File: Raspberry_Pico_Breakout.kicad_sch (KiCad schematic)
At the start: 13 parts, among them J1 Conn_01x20, J2 Conn_01x20, J3 Conn_01x20, J4 Conn_01x20, J5 Conn_01x20, J6 Conn_01x20, J7 Conn_01x20, J8 Conn_01x20

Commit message: doc: updated part documentation, schematics readability
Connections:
- no-connect marks 160 -> 0
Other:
- note added: "Female Header"
- note added: "For user"
- note added: "Left Socket for Pico"
- note added: "M3 Mounting holes"
- note added: "Male Headers"
- note added: "Pico IO Board"
- note added: "Right Socket for Pico"
- moved on the sheet: A1, J5

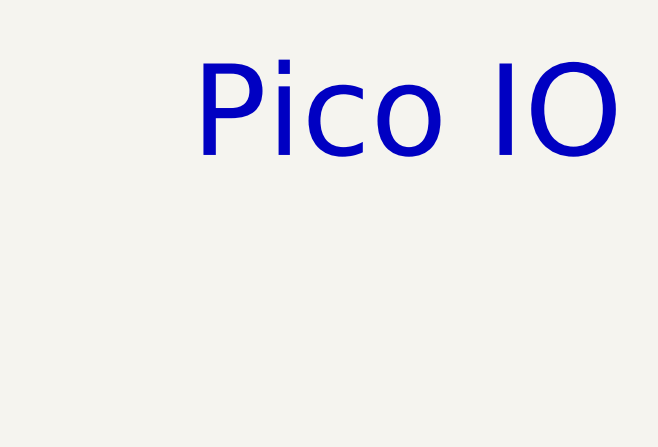
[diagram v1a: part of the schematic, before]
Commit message: doc: updated on schematic and PCB added license and design text
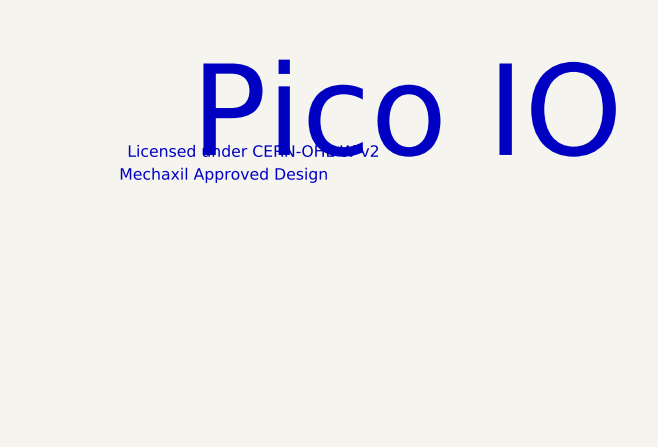
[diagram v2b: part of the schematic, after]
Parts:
- A1: now left out of the parts list
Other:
- note added: "Licensed under CERN-OHL-W v2"
- note added: "Mechaxil Approved Design"
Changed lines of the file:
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@@
 		)
 	)
+	(text "Licensed under CERN-OHL-W v2"
+		(exclude_from_sim no)
+		(at 35.814 32.004 0)
+		(effects
+			(font
+				(size 1.27 1.27)
+			)
+		)
+	)
 	(text "Pico IO Board"
 		(exclude_from_sim no)
@@
 		)
 	)
+	(text "Mechaxil Approved Design"
+		(exclude_from_sim no)
+		(at 32.512 34.544 0)
+		(effects
+			(font
+				(size 1.27 1.27)
+			)
+		)
+	)
 	(text "Female Header"
 		(exclude_from_sim no)
@@
 			)
 		)
-		(property "Datasheet" "https://octopart.com/datasheet/connfly/DS1023-1%2A20S21"
+		(property "Datasheet" "~"
 			(at 99.06 104.14 0)
 			(effects
@@
 		(unit 1)
 		(exclude_from_sim no)
-		(in_bom yes)
+		(in_bom no)
 		(on_board no)
 		(dnp no)

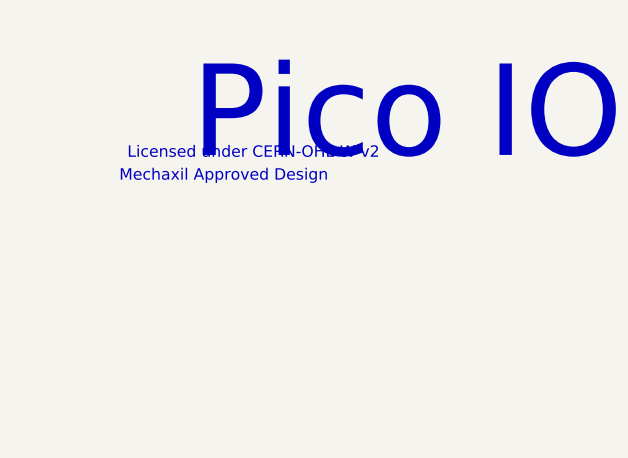
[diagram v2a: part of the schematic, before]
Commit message: major: upgrade to KiCAD 10.0 and OSHW License
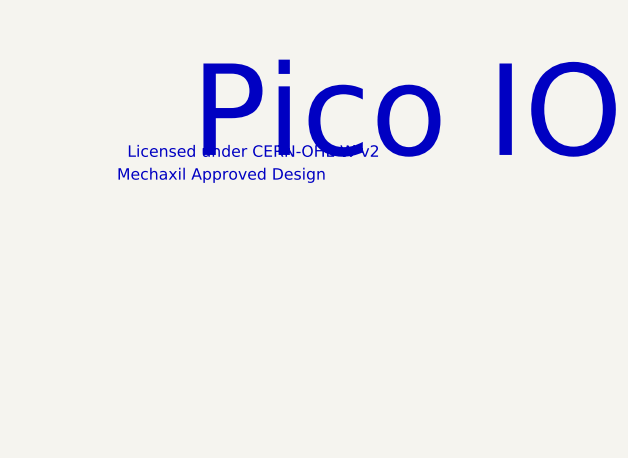
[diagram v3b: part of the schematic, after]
